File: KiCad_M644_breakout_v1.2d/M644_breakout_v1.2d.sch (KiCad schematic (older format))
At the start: 62 parts, among them IC1 ATMEGA16/32/644/1284, IC2 KIA7805A, Q1 16Mhz, SW1/PC5/21 SMD_TACT_4x4, X2 DG300-5.0-02P-12

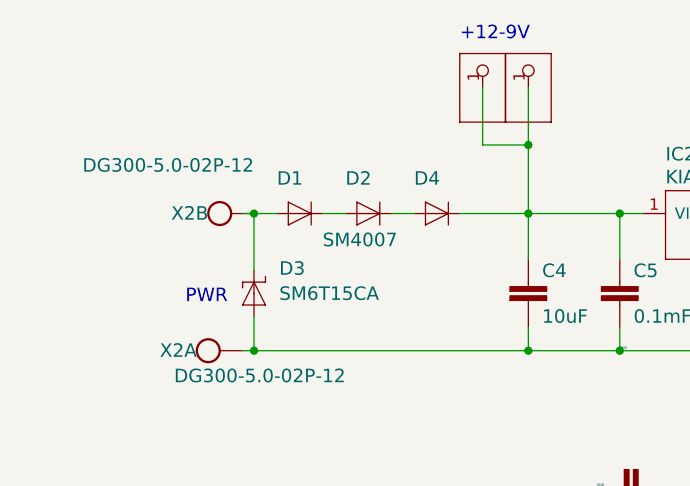
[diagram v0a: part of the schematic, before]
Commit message: Remove 3 diodes
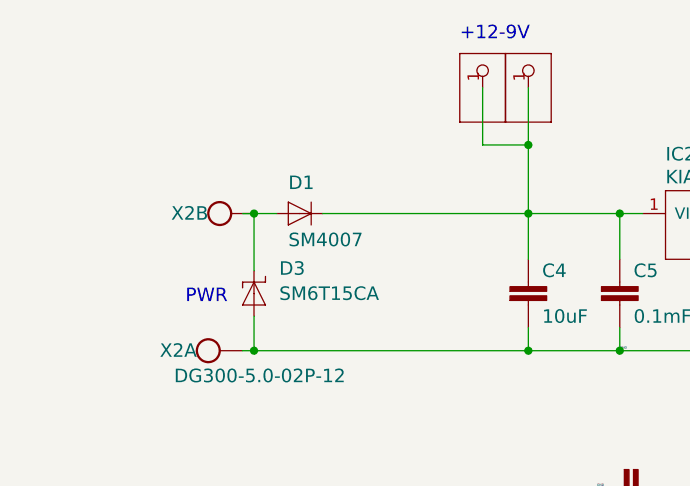
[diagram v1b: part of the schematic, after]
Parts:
- removed D2, D4: SM4007, M644_breakout_v1.2d:DO214AA, symbol M644_breakout_v1.2d-eagle-import:DIODE-DO214AA
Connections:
- net at C4.P$1 (1), C5.P$1 (1), IC2.1 (VI)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: now also D1.C
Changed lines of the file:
@@
 Wire Wire Line
 	2900 2000 2900 1800
-Wire Wire Line
-	2600 1800 2900 1800
 Connection ~ 2900 1500
 Connection ~ 3300 1800
 Connection ~ 2900 1800
-Wire Wire Line
-	2300 1800 2400 1800
 Wire Wire Line
 	9000 5800 8900 5800
@@
 P 1500 1800
 F 0 "X2" H 1500 1835 59  0000 R TNN
-F 1 "DG300-5.0-02P-12" H 1700 2045 59  0000 R TNN
+F 1 "DG300-5.0-02P-12" H 1700 2045 59  0001 R TNN
 F 2 "M644_breakout_v1.2d:W237-102" H 1500 1800 50  0001 C CNN
 F 3 "" H 1500 1800 50  0001 C CNN
@@
 U 1 0 C7EBFCBF
 P 1900 1800
-F 0 "D1" H 1800 1919 59  0000 L BNN
-F 1 "SM4007" H 2000 1650 59  0000 L BNN
+F 0 "D1" H 1850 1900 59  0000 L BNN
+F 1 "SM4007" H 1850 1650 59  0000 L BNN
 F 2 "M644_breakout_v1.2d:DO214AA" H 1900 1800 50  0001 C CNN
 F 3 "" H 1900 1800 50  0001 C CNN
 	1    1900 1800
-	1    0    0    -1
-$EndComp
-$Comp
-L M644_breakout_v1.2d-eagle-import:DIODE-DO214AA D2
-U 1 0 0CCA2570
-P 2200 1800
-F 0 "D2" H 2100 1919 59  0000 L BNN
-F 1 "SM4007" H 2250 1650 59  0001 L BNN
-F 2 "M644_breakout_v1.2d:DO214AA" H 2200 1800 50  0001 C CNN
-F 3 "" H 2200 1800 50  0001 C CNN
-	1    2200 1800
-	1    0    0    -1
-$EndComp
-$Comp
-L M644_breakout_v1.2d-eagle-import:DIODE-DO214AA D4
-U 1 0 0427F97B
-P 2500 1800
-F 0 "D4" H 2400 1919 59  0000 L BNN
-F 1 "SM4007" H 2430 1529 59  0001 L BNN
-F 2 "M644_breakout_v1.2d:DO214AA" H 2500 1800 50  0001 C CNN
-F 3 "" H 2500 1800 50  0001 C CNN
-	1    2500 1800
 	1    0    0    -1
 $EndComp
@@
 Wire Wire Line
 	2900 1500 2900 1800
-Wire Wire Line
-	2000 1800 2100 1800
 Text GLabel 8600 1900 0    50   Input ~ 0
 SCK
@@
 Wire Wire Line
 	8800 6100 8750 6100
+Wire Wire Line
+	2000 1800 2900 1800
 Wire Bus Line
 	7100 2250 7100 6550

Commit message: Slightly corrected schematic layout
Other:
- moved on the sheet: C1, C10, C11, C12, C2, C3, C4, C5, C6, C7, C8, C9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
